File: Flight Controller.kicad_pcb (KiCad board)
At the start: 6 copper layers, 39.5 x 39.5 mm, 151 parts, among them IC2 AT7456E, J1 Conn_01x08_MountingPin, J2 USB_C_Receptacle_USB2.0_14P, Q2 BC817W, SW1 SW_SPST, U1 AT32F435RGT7, U2 LMR51430, U3 BMP280, U4 SPX3819M5-L-3-3, U5 LMR51430, U6 W25Q128JVSIQ TR, U7 ICM-42688-P, U8 SPX3819M5-L-3-3, Y1 8M, Y2 27M

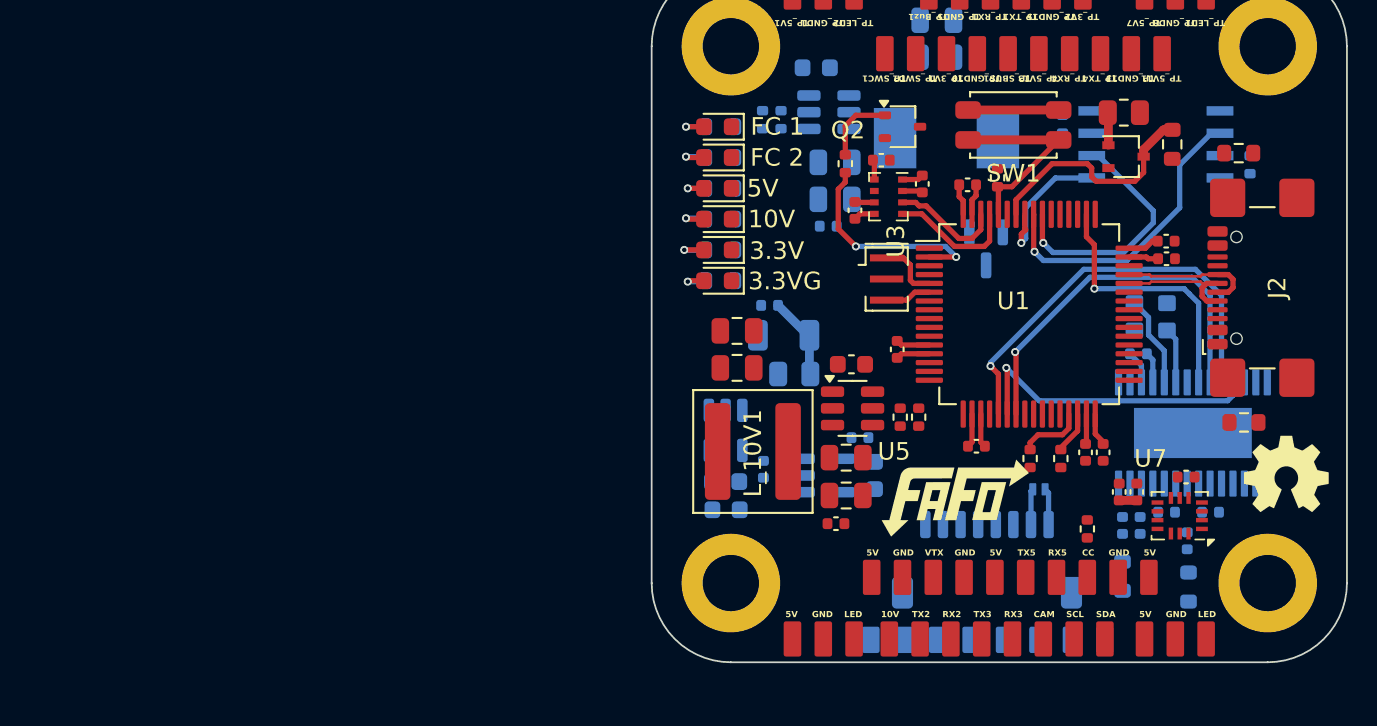
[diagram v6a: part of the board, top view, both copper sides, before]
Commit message: Power Supply Layout
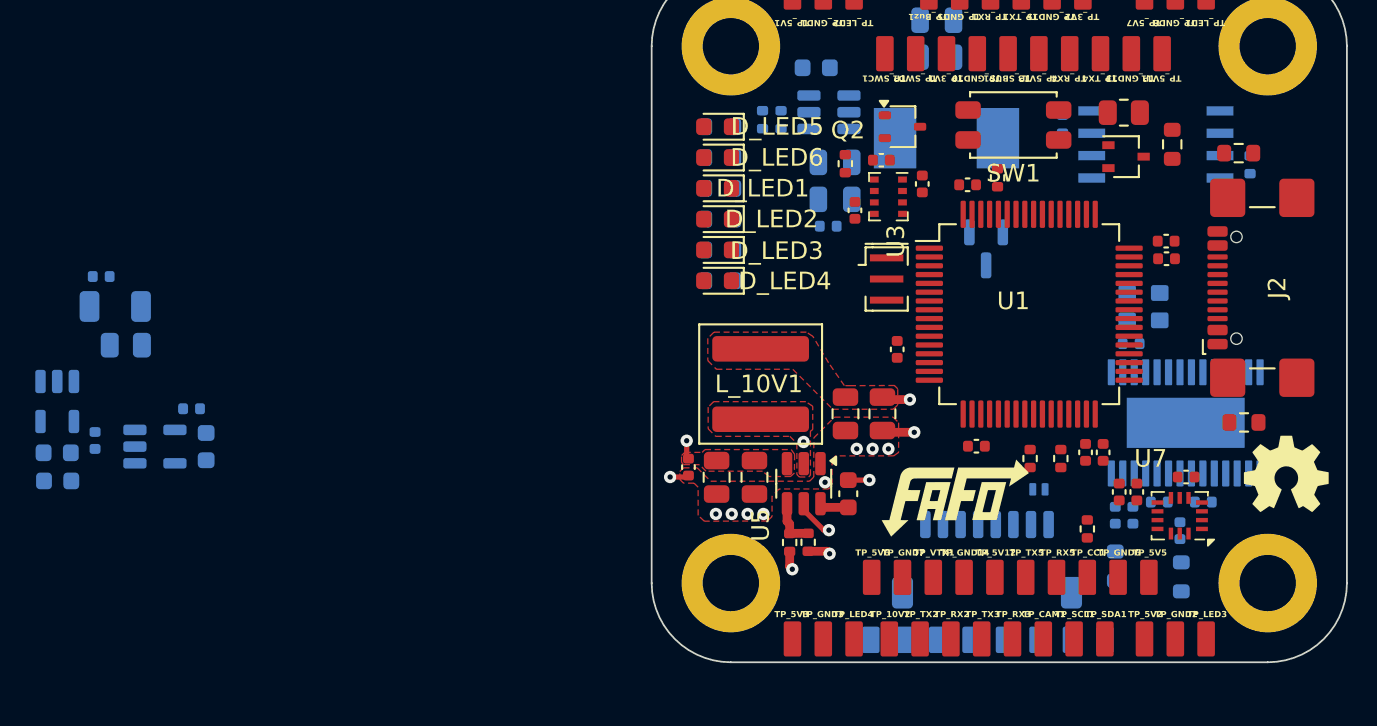
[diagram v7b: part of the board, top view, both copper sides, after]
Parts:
- D_LED5: renamed from FC 1
- D_LED6: renamed from FC 2
- moved C_3VG2 38.0 mm to (99.1, 90.4)
- moved C_3V2 38.0 mm to (93.6, 92.2)
- moved C_3VG1 38.0 mm to (99.9, 92.6)
- moved C_DEC1 38.0 mm to (91.5, 94.5)
- moved R_VBAT1 38.0 mm to (95.4, 86.8)
- moved R_VBAT2 38.0 mm to (94.8, 84.6)
- moved U8 38.0 mm to (97.0, 92.6)
- moved C_3V1 38.0 mm to (91.5, 92.9)
- moved C_VBAT1 38.0 mm to (94.0, 82.9)
- moved U4 38.0 mm to (91.5, 90.0)
- moved COUT_10V1 9.51 mm to (138.4, 90.7), turned to -90 degrees
- moved RFBT_10V1 9.49 mm to (133.1, 98.0), turned to 90 degrees
- moved RFBB_10V1 9.49 mm to (134.1, 98.0), turned to -90 degrees
- moved CIN_10V3 8.97 mm to (127.3, 93.7), turned to 90 degrees
- moved CIN_10V2 7.43 mm to (128.9, 94.3), turned to -90 degrees
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- renumbered 5V to D_LED1, 10V to D_LED2, 3.3V to D_LED3, 3.3VG to D_LED4, 10V to TP_10V2, 5V to TP_5V12, 5V to TP_5V2, 5V to TP_5V3, 5V to TP_5V5, 5V to TP_5V6, CAM to TP_CAM1, CC to TP_CC1, GND to TP_GND14, GND to TP_GND2, GND to TP_GND3, GND to TP_GND6, GND to TP_GND7, LED to TP_LED3, LED to TP_LED4, RX2 to TP_RX2, RX3 to TP_RX3, RX5 to TP_RX5, SCL to TP_SCL1, SDA to TP_SDA1, TX2 to TP_TX2, TX3 to TP_TX3, TX5 to TP_TX5, VTX to TP_VTX1
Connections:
- net Net-(U5-SW) renamed /SW
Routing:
- net /OSD_SCLK: track 24.0 -> 0.00 mm, vias 1 -> 0
- net /OSD_MOSI: track 21.8 -> 0.00 mm, vias 1 -> 0
- net +3.3V: track 18.8 -> 0.00 mm
- net +10V: track 0.00 -> 18.7 mm, vias 0 -> 2
- net /FLASH_MISO: track 17.3 -> 0.00 mm, vias 1 -> 0
- net /OSD_MISO: track 17.2 -> 0.00 mm, vias 1 -> 0
- net /OSD_CS: track 15.2 -> 0.00 mm, vias 1 -> 0
- net /FLASH_SCLK: track 14.3 -> 0.00 mm, vias 1 -> 0
- net /UART1_TX: track 13.2 -> 0.00 mm
- net /BUZ: track 12.2 -> 0.00 mm, vias 2 -> 0
- net /VBAT+: track 2.08 -> 13.5 mm, vias 0 -> 2
- net /BOOT: track 11.3 -> 0.00 mm
- net /FLASH_MOSI: track 8.30 -> 0.00 mm, vias 1 -> 0
- net /D-: track 7.55 -> 0.00 mm
- net /D+: track 7.55 -> 0.00 mm
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- added copper zone on F.Cu, net +10V
- added copper zone on F.Cu, net /SW
- added copper zone on F.Cu, net /VBAT+
- added copper zone on F.Cu, net GND
- added copper zone on In1.Cu, net GND

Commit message: Layout
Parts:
- moved C_3V2 56.0 mm to (149.3, 86.2)
- moved C_DEC1 56.0 mm to (147.2, 88.5)
- moved C_3V1 56.0 mm to (147.2, 86.9)
- moved U4 56.0 mm to (147.2, 84.0)
- moved C_VBAT1 55.0 mm to (148.1, 92.6), turned to 180 degrees
- moved R_VBAT2 52.9 mm to (147.3, 90.9), turned to 0 degrees
- moved R_VBAT1 47.9 mm to (143.1, 90.9)
- moved U8 44.2 mm to (140.4, 84.5), turned to -90 degrees
- moved C_3VG2 43.7 mm to (142.6, 86.5), turned to -90 degrees
- moved C_3VG1 40.8 mm to (140.4, 87.4), turned to 0 degrees
- moved R_LED1 12.6 mm to (130.4, 90.5)
- moved R_LED2 12.6 mm to (130.4, 92.2)
- moved R_LED3 12.6 mm to (130.4, 94.0)
- moved R_LED4 12.6 mm to (130.4, 95.7)
- moved R_LED5 12.6 mm to (130.4, 87.0)
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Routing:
- net GND: track 13.6 -> 2.18 mm, vias 11 -> 10
- net +10V: track 18.7 -> 16.4 mm
